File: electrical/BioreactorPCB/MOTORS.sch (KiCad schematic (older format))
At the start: 8 parts, among them J5 OSTTC022162, J7 OSTTC042162, J9 OSTTC042162, U1 L293D

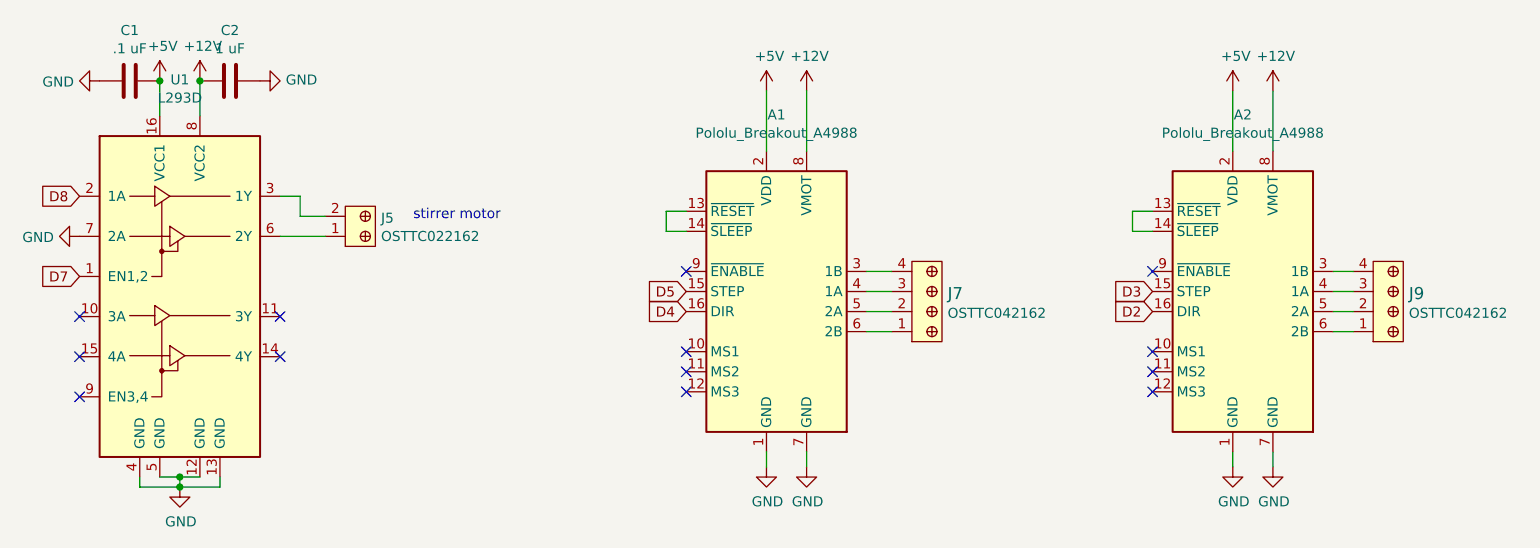
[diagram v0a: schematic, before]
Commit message: added missing electrolytic capacitors for A4988 breakouts. Preliminary layout now in place
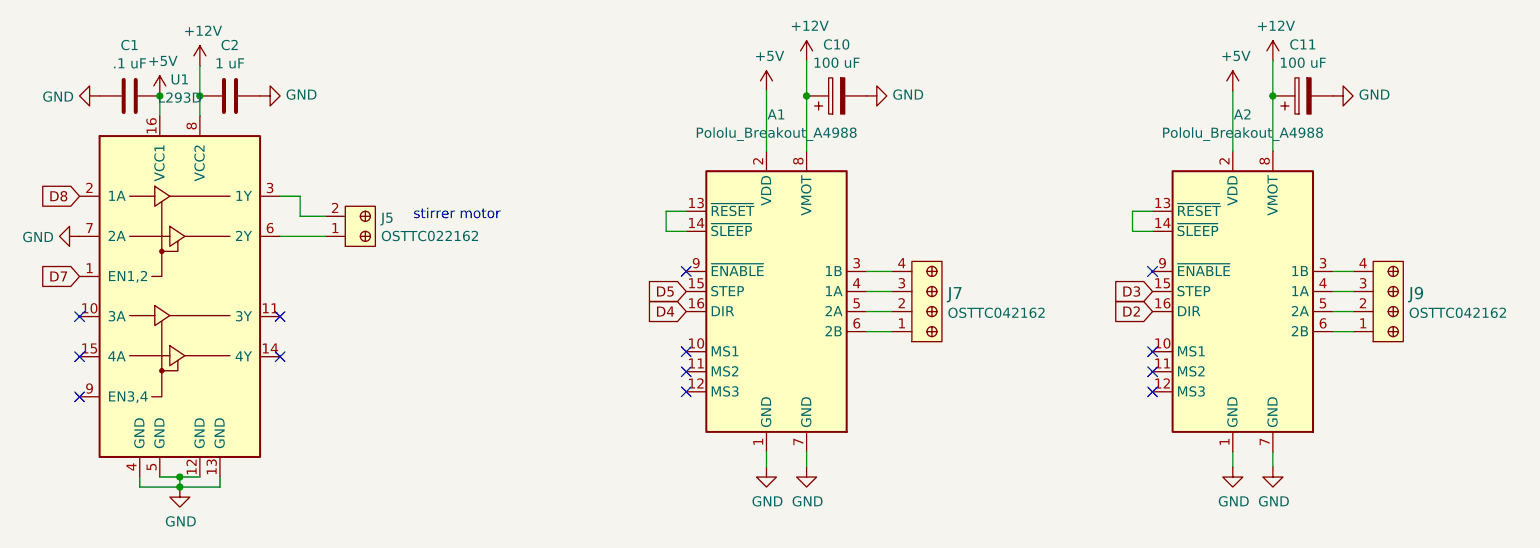
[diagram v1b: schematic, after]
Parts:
- added C10, C11: 100 uF, Capacitor_THT:CP_Radial_D5.0mm_P2.50mm, symbol Device:CP
- C1, C2: footprint Capacitor_THT:CP_Radial_Tantal_D5.0mm_P2.50mm -> Capacitor_THT:C_Disc_D5.0mm_W2.5mm_P2.50mm
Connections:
- net +12V: now also C10.1, C11.1
- net GND: now also C10.2, C11.2
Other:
- moved on the sheet: C1, C2
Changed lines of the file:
@@
 L Device:C C1
 U 1 1 62048E4E
-P 2400 2075
-F 0 "C1" V 2148 2075 50  0000 C CNN
-F 1 ".1 uF" V 2239 2075 50  0000 C CNN
-F 2 "Capacitor_THT:CP_Radial_Tantal_D5.0mm_P2.50mm" H 2438 1925 50  0001 C CNN
-F 3 "~" H 2400 2075 50  0001 C CNN
-	1    2400 2075
+P 2400 2150
+F 0 "C1" V 2148 2150 50  0000 C CNN
+F 1 ".1 uF" V 2239 2150 50  0000 C CNN
+F 2 "Capacitor_THT:C_Disc_D5.0mm_W2.5mm_P2.50mm" H 2438 2000 50  0001 C CNN
+F 3 "~" H 2400 2150 50  0001 C CNN
+	1    2400 2150
 	0    1    1    0
 $EndComp
@@
 L Device:C C2
 U 1 1 62048E54
-P 2900 2075
-F 0 "C2" V 2648 2075 50  0000 C CNN
-F 1 "1 uF" V 2739 2075 50  0000 C CNN
-F 2 "Capacitor_THT:CP_Radial_Tantal_D5.0mm_P2.50mm" H 2938 1925 50  0001 C CNN
-F 3 "~" H 2900 2075 50  0001 C CNN
-	1    2900 2075
+P 2900 2150
+F 0 "C2" V 2648 2150 50  0000 C CNN
+F 1 "1 uF" V 2739 2150 50  0000 C CNN
+F 2 "Capacitor_THT:C_Disc_D5.0mm_W2.5mm_P2.50mm" H 2938 2000 50  0001 C CNN
+F 3 "~" H 2900 2150 50  0001 C CNN
+	1    2900 2150
 	0    1    1    0
 $EndComp
 Wire Wire Line
-	2550 2075 2550 2250
-Wire Wire Line
-	2750 2250 2750 2075
+	2550 2150 2550 2250
+Wire Wire Line
+	2750 2250 2750 2150
 $Comp
 L power:+5V #PWR0108
 U 1 1 62048E5C
-P 2550 2075
-F 0 "#PWR0108" H 2550 1925 50  0001 C CNN
-F 1 "+5V" H 2565 2248 50  0000 C CNN
-F 2 "" H 2550 2075 50  0001 C CNN
-F 3 "" H 2550 2075 50  0001 C CNN
-	1    2550 2075
+P 2550 2150
+F 0 "#PWR0108" H 2550 2000 50  0001 C CNN
+F 1 "+5V" H 2565 2323 50  0000 C CNN
+F 2 "" H 2550 2150 50  0001 C CNN
+F 3 "" H 2550 2150 50  0001 C CNN
+	1    2550 2150
 	1    0    0    -1
 $EndComp
@@
 L power:+12V #PWR0109
 U 1 1 62048E62
-P 2750 2075
-F 0 "#PWR0109" H 2750 1925 50  0001 C CNN
-F 1 "+12V" H 2765 2248 50  0000 C CNN
-F 2 "" H 2750 2075 50  0001 C CNN
-F 3 "" H 2750 2075 50  0001 C CNN
-	1    2750 2075
-	1    0    0    -1
-$EndComp
-Connection ~ 2550 2075
-Connection ~ 2750 2075
+P 2750 2000
+F 0 "#PWR0109" H 2750 1850 50  0001 C CNN
+F 1 "+12V" H 2765 2173 50  0000 C CNN
+F 2 "" H 2750 2000 50  0001 C CNN
+F 3 "" H 2750 2000 50  0001 C CNN
+	1    2750 2000
+	1    0    0    -1
+$EndComp
+Connection ~ 2550 2150
 $Comp
 L power:GND #PWR0110
 U 1 1 62048E6A
-P 2250 2075
-F 0 "#PWR0110" H 2250 1825 50  0001 C CNN
-F 1 "GND" V 2255 1947 50  0000 R CNN
-F 2 "" H 2250 2075 50  0001 C CNN
-F 3 "" H 2250 2075 50  0001 C CNN
-	1    2250 2075
+P 2250 2150
+F 0 "#PWR0110" H 2250 1900 50  0001 C CNN
+F 1 "GND" V 2255 2022 50  0000 R CNN
+F 2 "" H 2250 2150 50  0001 C CNN
+F 3 "" H 2250 2150 50  0001 C CNN
+	1    2250 2150
 	0    1    1    0
 $EndComp
@@
 L power:GND #PWR0111
 U 1 1 62048E70
-P 3050 2075
-F 0 "#PWR0111" H 3050 1825 50  0001 C CNN
-F 1 "GND" V 3055 1947 50  0000 R CNN
-F 2 "" H 3050 2075 50  0001 C CNN
-F 3 "" H 3050 2075 50  0001 C CNN
-	1    3050 2075
+P 3050 2150
+F 0 "#PWR0111" H 3050 1900 50  0001 C CNN
+F 1 "GND" V 3055 2022 50  0000 R CNN
+F 2 "" H 3050 2150 50  0001 C CNN
+F 3 "" H 3050 2150 50  0001 C CNN
+	1    3050 2150
 	0    -1   -1   0
 $EndComp
@@
 $EndComp
 Wire Wire Line
-	5775 2425 5775 2125
+	5775 2425 5775 2150
 $Comp
 L power:+12V #PWR?
 U 1 1 62057077
-P 5775 2125
+P 5775 1975
 AR Path="/62057077" Ref="#PWR?"  Part="1"
 AR Path="/6200BC19/62057077" Ref="#PWR0112"  Part="1"
-F 0 "#PWR0112" H 5775 1975 50  0001 C CNN
-F 1 "+12V" H 5790 2298 50  0000 C CNN
-F 2 "" H 5775 2125 50  0001 C CNN
-F 3 "" H 5775 2125 50  0001 C CNN
-	1    5775 2125
+F 0 "#PWR0112" H 5775 1825 50  0001 C CNN
+F 1 "+12V" H 5790 2148 50  0000 C CNN
+F 2 "" H 5775 1975 50  0001 C CNN
+F 3 "" H 5775 1975 50  0001 C CNN
+	1    5775 1975
 	1    0    0    -1
 $EndComp
@@
 L power:+12V #PWR?
 U 1 1 6205DF81
-P 8100 2125
+P 8100 1975
 AR Path="/6205DF81" Ref="#PWR?"  Part="1"
 AR Path="/6200BC19/6205DF81" Ref="#PWR0121"  Part="1"
-F 0 "#PWR0121" H 8100 1975 50  0001 C CNN
-F 1 "+12V" H 8115 2298 50  0000 C CNN
-F 2 "" H 8100 2125 50  0001 C CNN
-F 3 "" H 8100 2125 50  0001 C CNN
-	1    8100 2125
-	1    0    0    -1
-$EndComp
-Wire Wire Line
-	8100 2125 8100 2425
+F 0 "#PWR0121" H 8100 1825 50  0001 C CNN
+F 1 "+12V" H 8115 2148 50  0000 C CNN
+F 2 "" H 8100 1975 50  0001 C CNN
+F 3 "" H 8100 1975 50  0001 C CNN
+	1    8100 1975
+	1    0    0    -1
+$EndComp
+Wire Wire Line
+	8100 1975 8100 2150
 $Comp
 L power:GND #PWR?
@@
 Text GLabel 7500 3225 0    50   Input ~ 0
 D2
+$Comp
+L Device:CP C10
+U 1 1 61D60F5E
+P 5925 2150
+F 0 "C10" V 6180 2150 50  0000 C CNN
+F 1 "100 uF" V 6089 2150 50  0000 C CNN
+F 2 "Capacitor_THT:CP_Radial_D5.0mm_P2.50mm" H 5963 2000 50  0001 C CNN
+F 3 "~" H 5925 2150 50  0001 C CNN
+	1    5925 2150
+	0    -1   -1   0
+$EndComp
+Connection ~ 5775 2150
+Wire Wire Line
+	5775 2150 5775 1975
+$Comp
+L power:GND #PWR0144
+U 1 1 61D67C41
+P 6075 2150
+F 0 "#PWR0144" H 6075 1900 50  0001 C CNN
+F 1 "GND" V 6080 2022 50  0000 R CNN
+F 2 "" H 6075 2150 50  0001 C CNN
+F 3 "" H 6075 2150 50  0001 C CNN
+	1    6075 2150
+	0    -1   -1   0
+$EndComp
+$Comp
+L Device:CP C11
+U 1 1 61D6A259
+P 8250 2150
+F 0 "C11" V 8505 2150 50  0000 C CNN
+F 1 "100 uF" V 8414 2150 50  0000 C CNN
+F 2 "Capacitor_THT:CP_Radial_D5.0mm_P2.50mm" H 8288 2000 50  0001 C CNN
+F 3 "~" H 8250 2150 50  0001 C CNN
+	1    8250 2150
+	0    -1   -1   0
+$EndComp
+$Comp
+L power:GND #PWR0161
+U 1 1 61D6A25F
+P 8400 2150
+F 0 "#PWR0161" H 8400 1900 50  0001 C CNN
+F 1 "GND" V 8405 2022 50  0000 R CNN
+F 2 "" H 8400 2150 50  0001 C CNN
+F 3 "" H 8400 2150 50  0001 C CNN
+	1    8400 2150
+	0    -1   -1   0
+$EndComp
+Connection ~ 8100 2150
+Wire Wire Line
+	8100 2150 8100 2425
+Connection ~ 2750 2150
+Wire Wire Line
+	2750 2150 2750 2000
 $EndSCHEMATC

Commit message: Converted all nonpolarized resistors and capacitors to SMD. USB now has differential pairs that conform to design guidelines. Lots of traces, to what end? idk.
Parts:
- C1, C2: footprint Capacitor_THT:C_Disc_D5.0mm_W2.5mm_P2.50mm -> Capacitor_SMD:C_0603_1608Metric_Pad1.08x0.95mm_HandSolder
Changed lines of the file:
@@
 F 0 "C1" V 2148 2150 50  0000 C CNN
 F 1 ".1 uF" V 2239 2150 50  0000 C CNN
-F 2 "Capacitor_THT:C_Disc_D5.0mm_W2.5mm_P2.50mm" H 2438 2000 50  0001 C CNN
+F 2 "Capacitor_SMD:C_0603_1608Metric_Pad1.08x0.95mm_HandSolder" H 2438 2000 50  0001 C CNN
 F 3 "~" H 2400 2150 50  0001 C CNN
 	1    2400 2150
@@
 F 0 "C2" V 2648 2150 50  0000 C CNN
 F 1 "1 uF" V 2739 2150 50  0000 C CNN
-F 2 "Capacitor_THT:C_Disc_D5.0mm_W2.5mm_P2.50mm" H 2938 2000 50  0001 C CNN
+F 2 "Capacitor_SMD:C_0603_1608Metric_Pad1.08x0.95mm_HandSolder" H 2938 2000 50  0001 C CNN
 F 3 "~" H 2900 2150 50  0001 C CNN
 	1    2900 2150
